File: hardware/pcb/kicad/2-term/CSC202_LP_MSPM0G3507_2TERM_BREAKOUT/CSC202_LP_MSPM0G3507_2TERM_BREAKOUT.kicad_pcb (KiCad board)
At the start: 2 copper layers, 100 x 35 mm, 10 parts, among them J1 J_IN1/J_IN3, J2 J_IN4/J_IN2, J3 J_OUT1, J4 J_OUT3, J5 J_OUT4, J6 J_OUT2

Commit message: implemented kibot and mkdocs
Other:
- board text added: "LP-MSPM0G3507"
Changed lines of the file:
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@@
 	)
 	(paper "A4")
+	(title_block
+		(title "CSC_202_LP_MSPM0G3507_2TERM_BREAKOUT")
+		(date "2026-01-15")
+		(rev "A")
+		(company "Eli Bell")
+		(comment 1 "breadboard center dividers.")
+		(comment 2 "the LaunchPad and reroutes the GPIO headers into a dual-row format that straddle the ")
+		(comment 3 "strip breadoard, such as the JAMECO ValuePro WBU-204-R. It plugs into the underside of ")
+		(comment 4 "A breakout board for the TI MSPM0G3507 LaunchPad intended for use with a TWO terminal ")
+	)
 	(layers
 		(0 "F.Cu" signal)
@@
 		)
 		(fp_text user "${REFERENCE}"
-			(at -0.916151 1.082981 0)
+			(at -3.406827 -1.01 0)
 			(unlocked yes)
 			(layer "F.Fab")
+			(hide yes)
 			(effects
 				(font
@@
 			(at 1.16 0 0)
 			(layer "F.Fab")
+			(hide yes)
 			(effects
 				(font
@@
 			(at 0.06 4.76 0)
 			(layer "F.Fab")
+			(hide yes)
 			(effects
 				(font
@@
 			(at 0.06 -4.76 0)
 			(layer "B.Fab")
+			(hide yes)
 			(effects
 				(font
@@
 		(layer "B.SilkS")
 	)
+	(gr_rect
+		(start 131.71 35.306556)
+		(end 190.09 141.836556)
+		(stroke
+			(width 0.1)
+			(type dot)
+		)
+		(fill no)
+		(locked yes)
+		(layer "Cmts.User")
+	)
 	(gr_line
 		(start 189.14 80.99)
@@
 		(layer "Edge.Cuts")
 	)
-	(gr_rect
-		(start 131.744727 35.293)
-		(end 190.124727 141.823)
-		(stroke
-			(width 0.1)
-			(type dot)
-		)
-		(fill no)
-		(layer "User.1")
-	)
 	(gr_text "GND"
 		(at 164.397865 87.907644 0)
@@
 		)
 	)
+	(gr_text "LP-MSPM0G3507"
+		(at 147.677381 40.32 0)
+		(layer "Cmts.User")
+		(effects
+			(font
+				(size 2 2)
+				(thickness 0.25)
+			)
+			(justify left bottom)
+		)
+	)
+	(gr_text_box "DIMENSIONS ARE IN MILLIMETERS\nTOLERANCE ±0.1 mm"
+		(start 86.86 123.77)
+		(end 114.08 128.49)
+		(margins 1.0025 1.0025 1.0025 1.0025)
+		(layer "Dwgs.User")
+		(effects
+			(font
+				(size 1 1)
+				(thickness 0.15)
+			)
+			(justify left top)
+		)
+		(border yes)
+		(stroke
+			(width 0.1)
+			(type solid)
+		)
+	)
+	(dimension
+		(type orthogonal)
+		(layer "Dwgs.User")
+		(pts
+			(xy 178.208927 79.979798) (xy 178.208927 114.93)
+		)
+		(height -91.428927)
+		(orientation 1)
+		(format
+			(prefix "")
+			(suffix "")
+			(units 3)
+			(units_format 0)
+			(precision 4)
+			(override_value "35")
+			(suppress_zeroes yes)
+		)
+		(style
+			(thickness 0.1)
+			(arrow_length 1.27)
+			(text_position_mode 0)
+			(arrow_direction outward)
+			(extension_height 0.58642)
+			(extension_offset 0.5)
+			(keep_text_aligned yes)
+		)
+		(gr_text "35"
+			(at 85.63 97.454899 90)
+			(layer "Dwgs.User")
+			(effects
+				(font
+					(size 1 1)
+					(thickness 0.15)
+				)
+			)
+		)
+	)
+	(dimension
+		(type orthogonal)
+		(layer "Dwgs.User")
+		(pts
+			(xy 89.15 83.24) (xy 189.2 83.31)
+		)
+		(height -5.63)
+		(orientation 0)
+		(format
+			(prefix "")
+			(suffix "")
+			(units 3)
+			(units_format 0)
+			(precision 4)
+			(override_value "100")
+			(suppress_zeroes yes)
+		)
+		(style
+			(thickness 0.1)
+			(arrow_length 1.27)
+			(text_position_mode 0)
+			(arrow_direction outward)
+			(extension_height 0.58642)
+			(extension_offset 0.5)
+			(keep_text_aligned yes)
+		)
+		(gr_text "100"
+			(at 139.175 76.46 0)
+			(layer "Dwgs.User")
+			(effects
+				(font
+					(size 1 1)
+					(thickness 0.15)
+				)
+			)
+		)
+	)
+	(dimension
+		(type orthogonal)
+		(layer "Cmts.User")
+		(pts
+			(xy 131.71 35.306556) (xy 190.09 35.306556)
+		)
+		(height -4.046556)
+		(orientation 0)
+		(format
+			(prefix "")
+			(suffix "")
+			(units 3)
+			(units_format 0)
+			(precision 4)
+			(suppress_zeroes yes)
+		)
+		(style
+			(thickness 0.1)
+			(arrow_length 1.27)
+			(text_position_mode 0)
+			(arrow_direction outward)
+			(extension_height 0.58642)
+			(extension_offset 0.5)
+			(keep_text_aligned yes)
+		)
+		(gr_text "58.38"
+			(at 160.9 30.11 0)
+			(layer "Cmts.User")
+			(effects
+				(font
+					(size 1 1)
+					(thickness 0.15)
+				)
+			)
+		)
+	)
+	(dimension
+		(type orthogonal)
+		(layer "Cmts.User")
+		(pts
+			(xy 190.09 35.306556) (xy 190.09 141.836556)
+		)
+		(height 9.926731)
+		(orientation 1)
+		(format
+			(prefix "")
+			(suffix "")
+			(units 3)
+			(units_format 0)
+			(precision 4)
+			(suppress_zeroes yes)
+		)
+		(style
+			(thickness 0.1)
+			(arrow_length 1.27)
+			(text_position_mode 0)
+			(arrow_direction outward)
+			(extension_height 0.58642)
+			(extension_offset 0.5)
+			(keep_text_aligned yes)
+		)
+		(gr_text "106.53"
+			(at 198.866731 88.571556 90)
+			(layer "Cmts.User")
+			(effects
+				(font
+					(size 1 1)
+					(thickness 0.15)
+				)
+			)
+		)
+	)

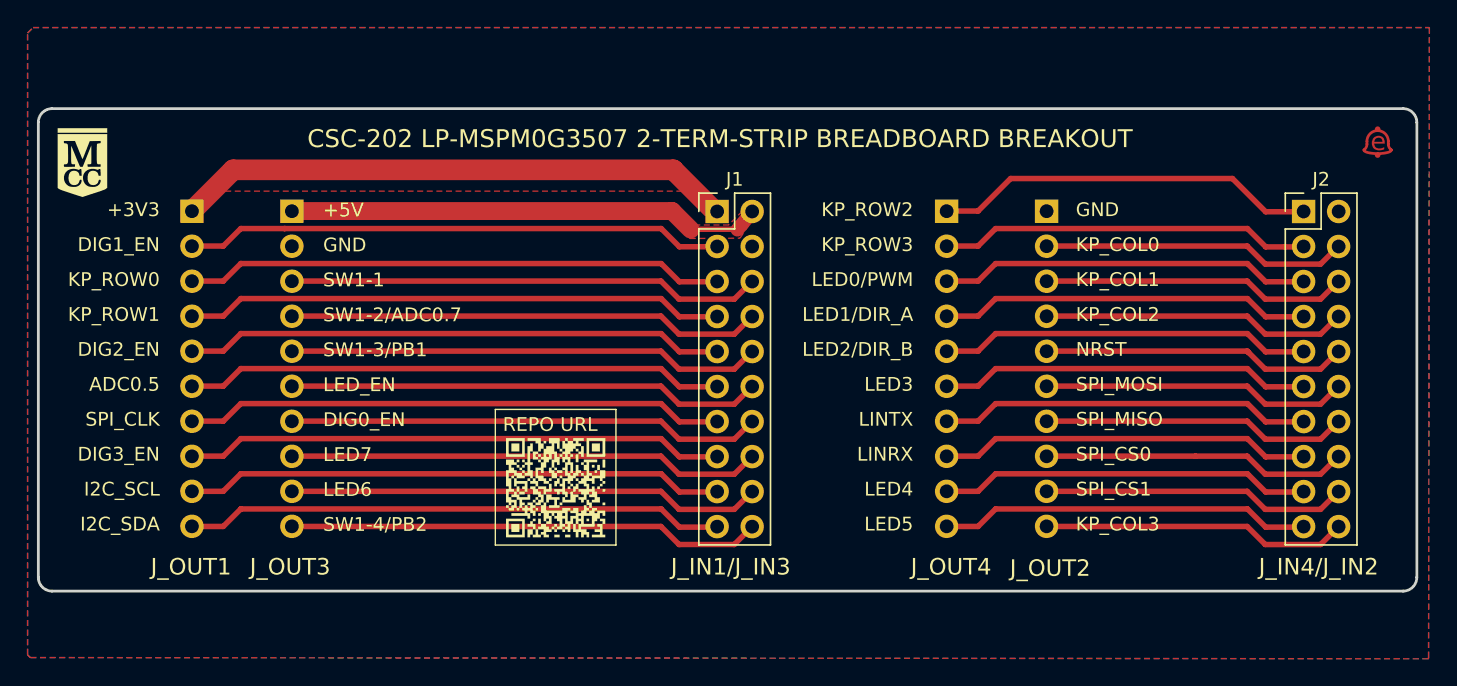
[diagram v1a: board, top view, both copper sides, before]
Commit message: init led module
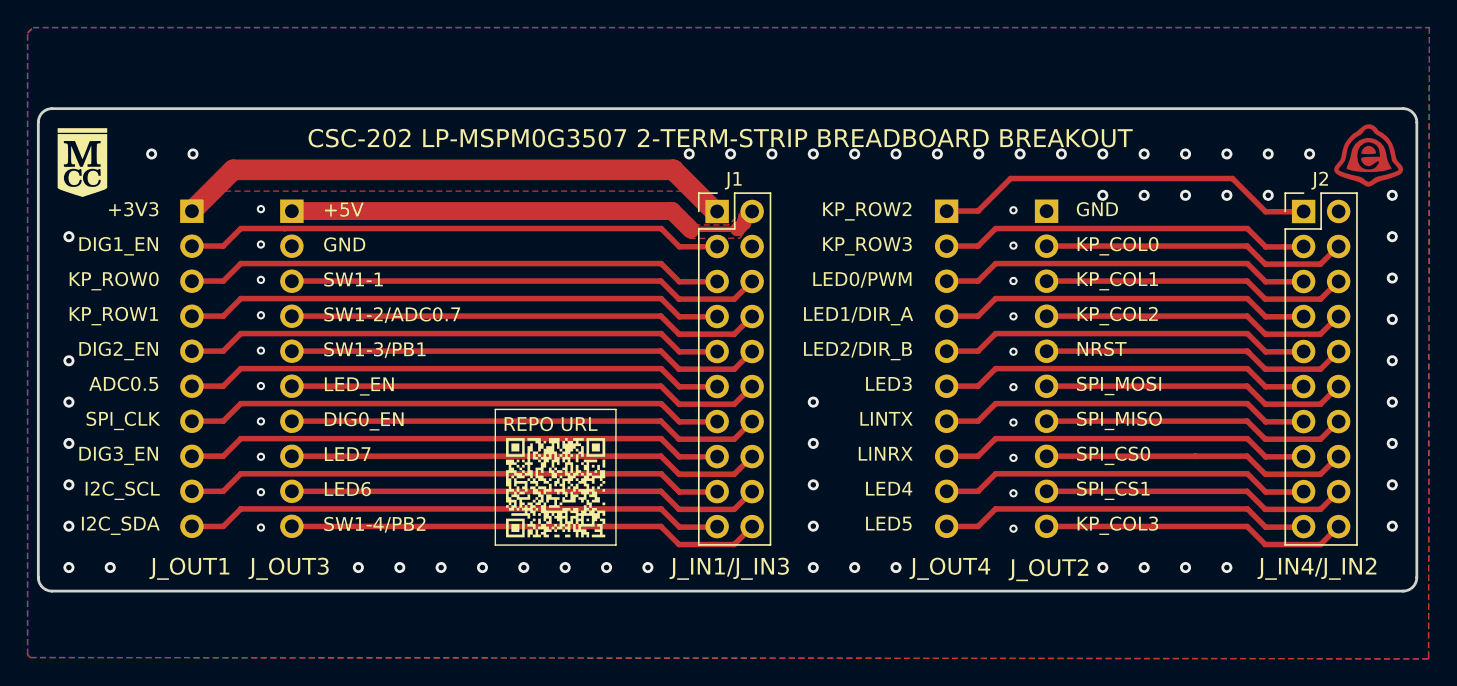
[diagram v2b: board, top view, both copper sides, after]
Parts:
- removed LOGO2: Logo, 01-Shared_Project_Footprints:Makers-Mark_Eli_Bell
- added G***: LOGO, Eli_Bell_Logo, F.Cu at (185.6, 83.4)
- G1, G2: footprint 01-Shared_Project_Footprints:Repo_URL_QR -> Repo_URL_QR
- J1: footprint 01-Shared_Project_Footprints:PinHeader_2x10_P2.54mm_Vertical_J1-J3 -> PinHeader_2x10_P2.54mm_Vertical_J1-J3
- J2: footprint 01-Shared_Project_Footprints:PinHeader_2x10_P2.54mm_Vertical_J2-J4 -> PinHeader_2x10_P2.54mm_Vertical_J2-J4
- J3, J4, J5, J6: footprint Connector_PinHeader_2.54mm:PinHeader_1x10_P2.54mm_Vertical -> PinHeader_1x10_P2.54mm_Vertical
- LOGO1: footprint 01-Shared_Project_Footprints:MCC-Logo -> MCC-Logo
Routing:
- net +5V: track 32.9 -> 34.7 mm
- net GND: vias 0 -> 79
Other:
- board text added: "{ "ViaStitching": "0.2", "stitch_zone_0": { "HSpacing": "1", "VSpacing": "1", "HOffset": "0", "VOffset": "0", "Clearance": "0", "Randomize": false } }"
- board text added: "{ "ViaStitching": "0.2", "stitch_zone_0": { "HSpacing": "3", "VSpacing": "3", "HOffset": "0", "VOffset": "0", "Clearance": ".2", "Randomize": false } }"
